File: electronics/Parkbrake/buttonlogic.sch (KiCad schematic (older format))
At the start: 43 parts

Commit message: ordernr, type and footprints for all components
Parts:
- C? (x7): footprint (none) -> Capacitors_SMD:C_0805; farnell (none) -> 2496940; part (none) -> 0805B104J500CT
- C? (x2): footprint (none) -> Capacitors_SMD:c_elec_4x5.3; symbol C -> CP; farnell (none) -> 2069144; part (none) -> EXV336M6R3A9BAA
- D? (x4): footprint (none) -> Diodes_SMD:SOD-123; farnell (none) -> 2454044; part (none) -> MMSZ4684
- D? (x7): footprint (none) -> Diodes_SMD:SOD-123; farnell (none) -> 2433353; part (none) -> 1N4148W-E3-08
- Q?: value Q_PMOS_GSD -> BSS308; footprint (none) -> TO_SOT_Packages_SMD:SOT-23; farnell (none) -> 2432719; part (none) -> BSS308PE H6327
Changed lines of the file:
@@
 F 0 "D?" H 850 3175 50  0000 C CNN
 F 1 "3.3V" H 850 2975 50  0000 C CNN
-F 2 "" H 850 3075 50  0000 C CNN
+F 2 "Diodes_SMD:SOD-123" H 850 3075 50  0001 C CNN
 F 3 "" H 850 3075 50  0000 C CNN
+F 4 "MMSZ4684" H 850 3075 60  0001 C CNN "part"
+F 5 "2454044" H 850 3075 60  0001 C CNN "farnell"
 	1    850  3075
 	0    1    1    0
@@
 F 0 "C?" H 1475 3100 50  0000 L CNN
 F 1 "100n" H 1350 2975 50  0000 L CNN
-F 2 "" H 1363 2925 50  0000 C CNN
+F 2 "Capacitors_SMD:C_0805" H 1363 2925 50  0001 C CNN
 F 3 "" H 1325 3075 50  0000 C CNN
+F 4 "2496940" H 1325 3075 60  0001 C CNN "farnell"
+F 5 "0805B104J500CT" H 1325 3075 60  0001 C CNN "part"
 	1    1325 3075
 	1    0    0    -1
@@
 F 0 "D?" H 850 4425 50  0000 C CNN
 F 1 "3.3V" H 850 4225 50  0000 C CNN
-F 2 "" H 850 4325 50  0000 C CNN
+F 2 "Diodes_SMD:SOD-123" H 850 4325 50  0001 C CNN
 F 3 "" H 850 4325 50  0000 C CNN
+F 4 "MMSZ4684" H 850 4325 60  0001 C CNN "part"
+F 5 "2454044" H 850 4325 60  0001 C CNN "farnell"
 	1    850  4325
 	0    1    1    0
@@
 F 0 "C?" H 1450 4325 50  0000 L CNN
 F 1 "100n" H 1350 4225 50  0000 L CNN
-F 2 "" H 1363 4175 50  0000 C CNN
+F 2 "Capacitors_SMD:C_0805" H 1363 4175 50  0001 C CNN
 F 3 "" H 1325 4325 50  0000 C CNN
+F 4 "2496940" H 1325 4325 60  0001 C CNN "farnell"
+F 5 "0805B104J500CT" H 1325 4325 60  0001 C CNN "part"
 	1    1325 4325
 	1    0    0    -1
@@
 F 0 "D?" H 850 5425 50  0000 C CNN
 F 1 "3.3V" H 850 5225 50  0000 C CNN
-F 2 "" H 850 5325 50  0000 C CNN
+F 2 "Diodes_SMD:SOD-123" H 850 5325 50  0001 C CNN
 F 3 "" H 850 5325 50  0000 C CNN
+F 4 "MMSZ4684" H 850 5325 60  0001 C CNN "part"
+F 5 "2454044" H 850 5325 60  0001 C CNN "farnell"
 	1    850  5325
 	0    1    1    0
@@
 F 0 "C?" H 1450 5325 50  0000 L CNN
 F 1 "100n" H 1350 5225 50  0000 L CNN
-F 2 "" H 1363 5175 50  0000 C CNN
+F 2 "Capacitors_SMD:C_0805" H 1363 5175 50  0001 C CNN
 F 3 "" H 1325 5325 50  0000 C CNN
+F 4 "2496940" H 1325 5325 60  0001 C CNN "farnell"
+F 5 "0805B104J500CT" H 1325 5325 60  0001 C CNN "part"
 	1    1325 5325
 	1    0    0    -1
@@
 F 0 "D?" H 850 6425 50  0000 C CNN
 F 1 "3.3V" H 850 6225 50  0000 C CNN
-F 2 "" H 850 6325 50  0000 C CNN
+F 2 "Diodes_SMD:SOD-123" H 850 6325 50  0001 C CNN
 F 3 "" H 850 6325 50  0000 C CNN
+F 4 "MMSZ4684" H 850 6325 60  0001 C CNN "part"
+F 5 "2454044" H 850 6325 60  0001 C CNN "farnell"
 	1    850  6325
 	0    1    1    0
@@
 F 0 "C?" H 1350 6425 50  0000 L CNN
 F 1 "100n" H 1350 6225 50  0000 L CNN
-F 2 "" H 1363 6175 50  0000 C CNN
+F 2 "Capacitors_SMD:C_0805" H 1363 6175 50  0001 C CNN
 F 3 "" H 1325 6325 50  0000 C CNN
+F 4 "2496940" H 1325 6325 60  0001 C CNN "farnell"
+F 5 "0805B104J500CT" H 1325 6325 60  0001 C CNN "part"
 	1    1325 6325
 	1    0    0    -1
@@
 P 2025 6950
 F 0 "Q?" H 2325 7000 50  0000 R CNN
-F 1 "Q_PMOS_GSD" H 2675 6900 50  0000 R CNN
-F 2 "" H 2225 7050 50  0000 C CNN
+F 1 "BSS308" H 2500 6875 50  0000 R CNN
+F 2 "TO_SOT_Packages_SMD:SOT-23" H 2225 7050 50  0001 C CNN
 F 3 "" H 2025 6950 50  0000 C CNN
+F 4 "BSS308PE H6327" H 2025 6950 60  0001 C CNN "part"
+F 5 "2432719" H 2025 6950 60  0001 C CNN "farnell"
 	1    2025 6950
 	1    0    0    1
@@
 F 0 "D?" H 1575 6875 50  0000 C CNN
 F 1 "1n4148w" H 1575 6675 50  0000 C CNN
-F 2 "" H 1575 6775 50  0000 C CNN
+F 2 "Diodes_SMD:SOD-123" H 1575 6775 50  0001 C CNN
 F 3 "" H 1575 6775 50  0000 C CNN
+F 4 "1N4148W-E3-08" H 1575 6775 60  0001 C CNN "part"
+F 5 "2433353" H 1575 6775 60  0001 C CNN "farnell"
 	1    1575 6775
 	0    1    1    0
@@
 F 0 "D?" H 1350 2450 50  0000 C CNN
 F 1 "1n4148w" H 1300 2675 50  0000 C CNN
-F 2 "" H 1350 2550 50  0000 C CNN
+F 2 "Diodes_SMD:SOD-123" H 1350 2550 50  0001 C CNN
 F 3 "" H 1350 2550 50  0000 C CNN
+F 4 "1N4148W-E3-08" H 1350 2550 60  0001 C CNN "part"
+F 5 "2433353" H 1350 2550 60  0001 C CNN "farnell"
 	1    1350 2550
 	1    0    0    -1
@@
 F 0 "D?" H 1350 3700 50  0000 C CNN
 F 1 "1n4148w" H 1350 3900 50  0000 C CNN
-F 2 "" H 1375 3800 50  0000 C CNN
+F 2 "Diodes_SMD:SOD-123" H 1375 3800 50  0001 C CNN
 F 3 "" H 1375 3800 50  0000 C CNN
+F 4 "1N4148W-E3-08" H 1375 3800 60  0001 C CNN "part"
+F 5 "2433353" H 1375 3800 60  0001 C CNN "farnell"
 	1    1375 3800
 	1    0    0    -1
@@
 F 0 "D?" H 1375 4675 50  0000 C CNN
 F 1 "1n4148w" H 1425 4925 50  0000 C CNN
-F 2 "" H 1375 4800 50  0000 C CNN
+F 2 "Diodes_SMD:SOD-123" H 1375 4800 50  0001 C CNN
 F 3 "" H 1375 4800 50  0000 C CNN
+F 4 "1N4148W-E3-08" H 1375 4800 60  0001 C CNN "part"
+F 5 "2433353" H 1375 4800 60  0001 C CNN "farnell"
 	1    1375 4800
 	1    0    0    -1
@@
 F 0 "D?" H 1375 5675 50  0000 C CNN
 F 1 "1n4148w" H 1375 5925 50  0000 C CNN
-F 2 "" H 1375 5800 50  0000 C CNN
+F 2 "Diodes_SMD:SOD-123" H 1375 5800 50  0001 C CNN
 F 3 "" H 1375 5800 50  0000 C CNN
+F 4 "1N4148W-E3-08" H 1375 5800 60  0001 C CNN "part"
+F 5 "2433353" H 1375 5800 60  0001 C CNN "farnell"
 	1    1375 5800
 	1    0    0    -1
@@
 F 0 "D?" H 5975 3550 50  0000 C CNN
 F 1 "1n4148" H 6025 3350 50  0000 C CNN
-F 2 "" H 5975 3450 50  0000 C CNN
+F 2 "Diodes_SMD:SOD-123" H 5975 3450 50  0001 C CNN
 F 3 "" H 5975 3450 50  0000 C CNN
+F 4 "2433353" H 5975 3450 60  0001 C CNN "farnell"
+F 5 "1N4148W-E3-08" H 5975 3450 60  0001 C CNN "part"
 	1    5975 3450
 	1    0    0    -1
 $EndComp
 $Comp
-L C C?
+L CP C?
 U 1 1 578F3B8F
 P 6125 3100
 F 0 "C?" H 6150 3200 50  0000 L CNN
 F 1 "33uF" H 6150 3000 50  0000 L CNN
-F 2 "" H 6163 2950 50  0000 C CNN
+F 2 "Capacitors_SMD:c_elec_4x5.3" H 6163 2950 50  0001 C CNN
 F 3 "" H 6125 3100 50  0000 C CNN
+F 4 "2069144" H 6125 3100 60  0001 C CNN "farnell"
+F 5 "EXV336M6R3A9BAA" H 6125 3100 60  0001 C CNN "part"
 	1    6125 3100
 	1    0    0    -1
@@
 $EndComp
 $Comp
-L C C?
+L CP C?
 U 1 1 578F6B3F
 P 6125 4250
 F 0 "C?" H 6150 4350 50  0000 L CNN
 F 1 "33uF" H 6150 4150 50  0000 L CNN
-F 2 "" H 6163 4100 50  0000 C CNN
+F 2 "Capacitors_SMD:c_elec_4x5.3" H 6163 4100 50  0001 C CNN
 F 3 "" H 6125 4250 50  0000 C CNN
+F 4 "EXV336M6R3A9BAA" H 6125 4250 60  0001 C CNN "part"
+F 5 "2069144" H 6125 4250 60  0001 C CNN "farnell"
 	1    6125 4250
 	1    0    0    -1
@@
 F 0 "D?" H 5975 4750 50  0000 C CNN
 F 1 "1n4148w" H 5975 4550 50  0000 C CNN
-F 2 "" H 5975 4650 50  0000 C CNN
+F 2 "Diodes_SMD:SOD-123" H 5975 4650 50  0001 C CNN
 F 3 "" H 5975 4650 50  0000 C CNN
+F 4 "2433353" H 5975 4650 60  0001 C CNN "farnell"
+F 5 "1N4148W-E3-08" H 5975 4650 60  0001 C CNN "part"
 	1    5975 4650
 	1    0    0    -1
@@
 F 0 "C?" H 4150 6150 50  0000 L CNN
 F 1 "100n" H 4150 5950 50  0000 L CNN
-F 2 "" H 4163 5900 50  0000 C CNN
+F 2 "Capacitors_SMD:C_0805" H 4163 5900 50  0001 C CNN
 F 3 "" H 4125 6050 50  0000 C CNN
+F 4 "2496940" H 4125 6050 60  0001 C CNN "farnell"
+F 5 "0805B104J500CT" H 4125 6050 60  0001 C CNN "part"
 	1    4125 6050
 	1    0    0    -1
@@
 F 0 "C?" H 4425 6150 50  0000 L CNN
 F 1 "100n" H 4425 5950 50  0000 L CNN
-F 2 "" H 4438 5900 50  0000 C CNN
+F 2 "Capacitors_SMD:C_0805" H 4438 5900 50  0001 C CNN
 F 3 "" H 4400 6050 50  0000 C CNN
+F 4 "2496940" H 4400 6050 60  0001 C CNN "farnell"
+F 5 "0805B104J500CT" H 4400 6050 60  0001 C CNN "part"
 	1    4400 6050
 	1    0    0    -1
@@
 F 0 "C?" H 4700 6150 50  0000 L CNN
 F 1 "100n" H 4700 5950 50  0000 L CNN
-F 2 "" H 4713 5900 50  0000 C CNN
+F 2 "Capacitors_SMD:C_0805" H 4713 5900 50  0001 C CNN
 F 3 "" H 4675 6050 50  0000 C CNN
+F 4 "2496940" H 4675 6050 60  0001 C CNN "farnell"
+F 5 "0805B104J500CT" H 4675 6050 60  0001 C CNN "part"
 	1    4675 6050
 	1    0    0    -1

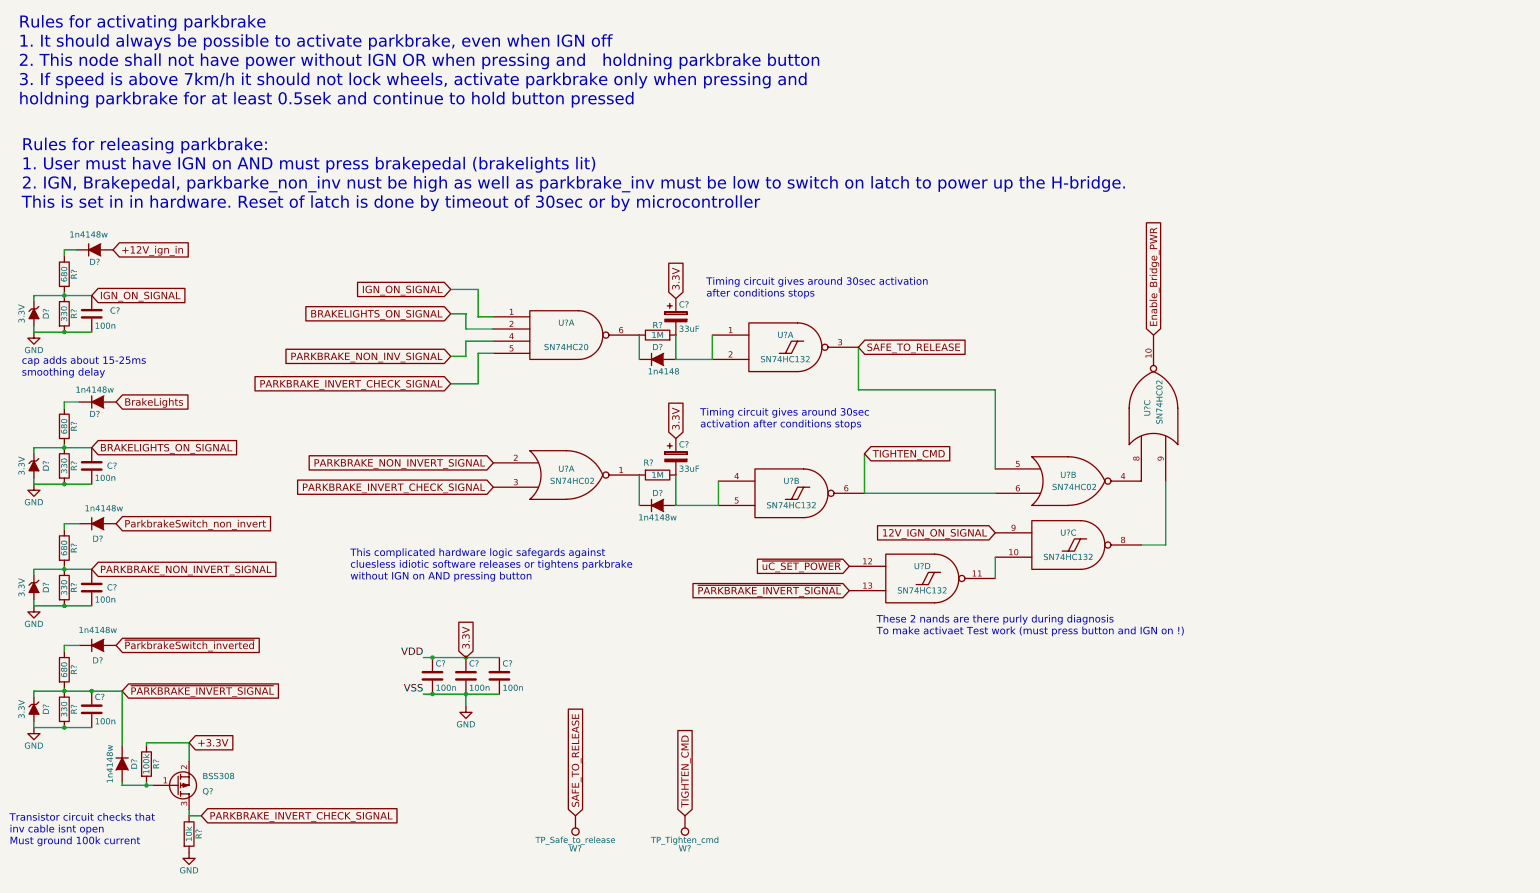
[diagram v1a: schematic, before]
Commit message: Make it pass DRC rule check
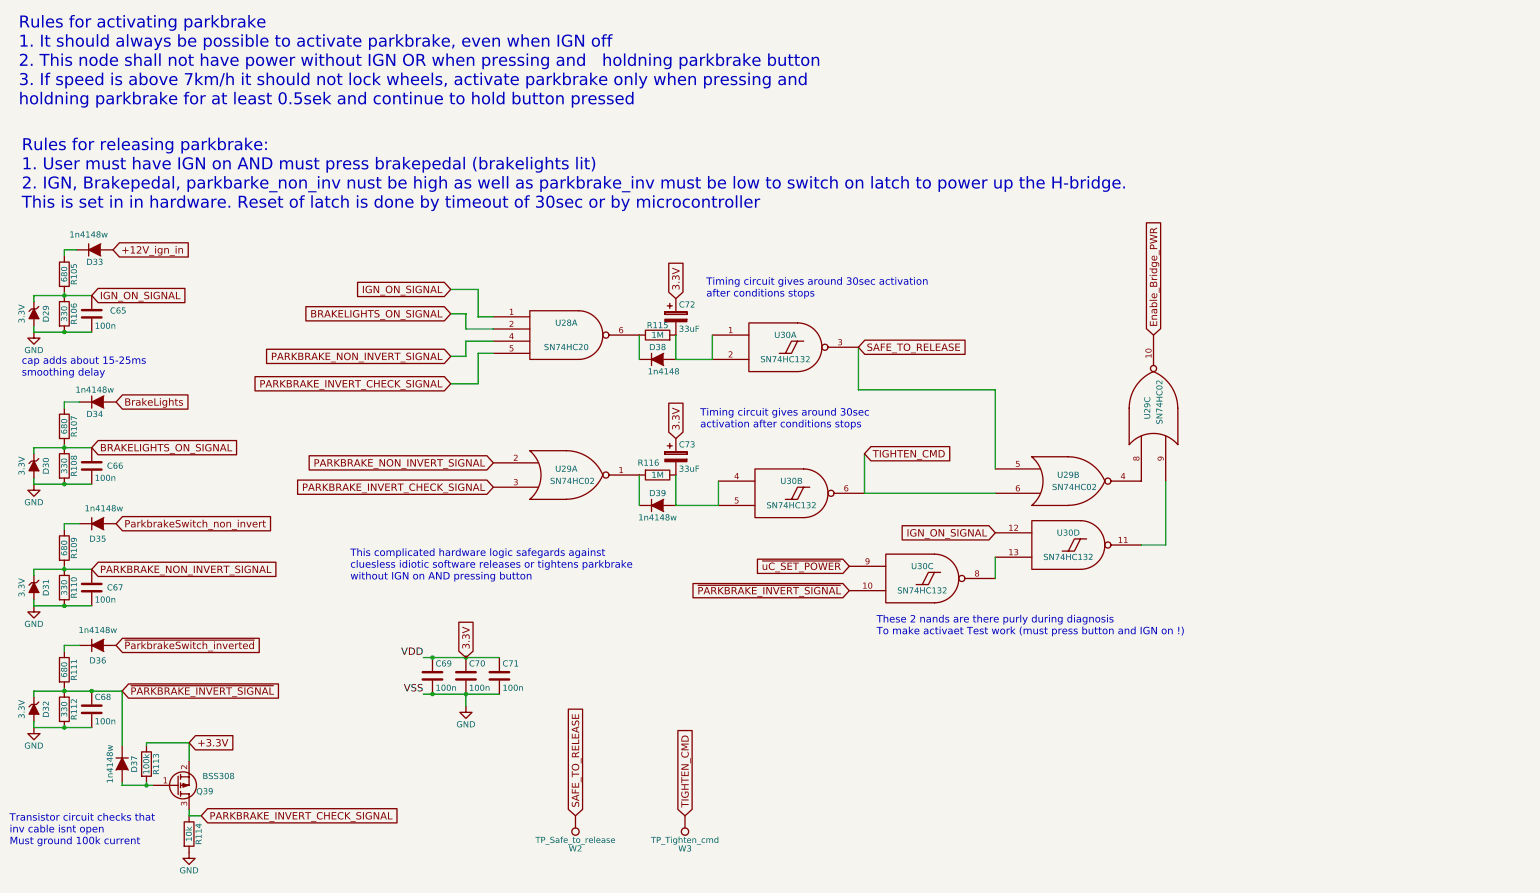
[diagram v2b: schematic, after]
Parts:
- gave numbers to parts that had none: 38
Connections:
- net PARKBRAKE_NON_INV_SIGNAL is gone; now on net PARKBRAKE_NON_INVERT_SIGNAL: U28.4
- net IGN_ON_SIGNAL: now also U30.12
- net ~PARKBRAKE_INVERT_SIGNAL: now also U30.10; no longer U30.13
- net ~uC_SET_POWER: now also U30.9; no longer U30.12
- net at U29.9: now also U30.11; no longer U30.8
- removed net 12V_IGN_ON_SIGNAL: U30.9
- new net: U30.13, U30.8
